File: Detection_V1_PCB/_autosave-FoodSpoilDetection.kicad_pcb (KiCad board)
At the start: 2 copper layers, 60 x 55 mm, 29 parts, among them J3 Conn_01x03_Socket, J4 Conn_01x03_Socket, J5 Conn_01x04_Socket, J6 Conn_01x03_Socket, J7 Conn_01x06_Socket, J9 Conn_01x10_Socket, Q1 AO3400A, Q2 AO3401A, Q3 AO3401A, U1 XIAO-ESP32-S3-DIP

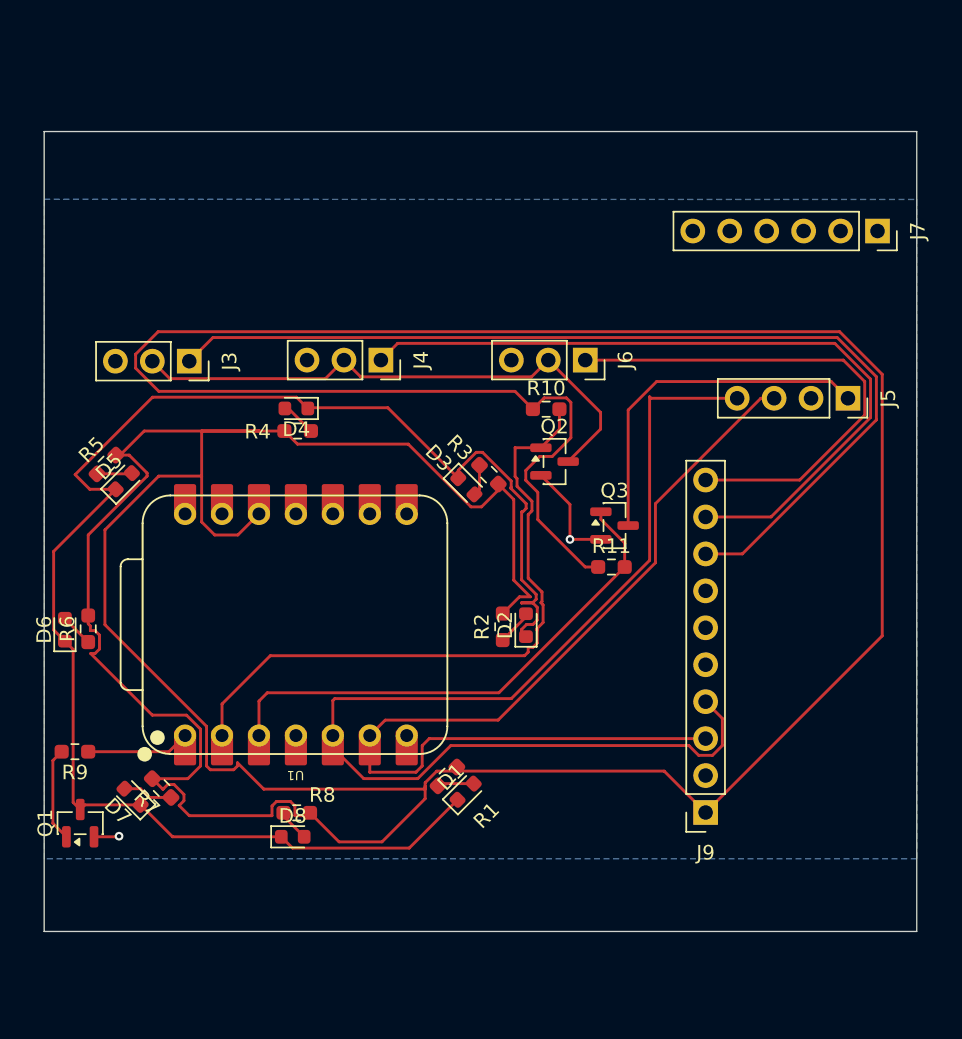
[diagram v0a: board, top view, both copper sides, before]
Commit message: added mounting holes
Need to align mounting holes and fiduciaries
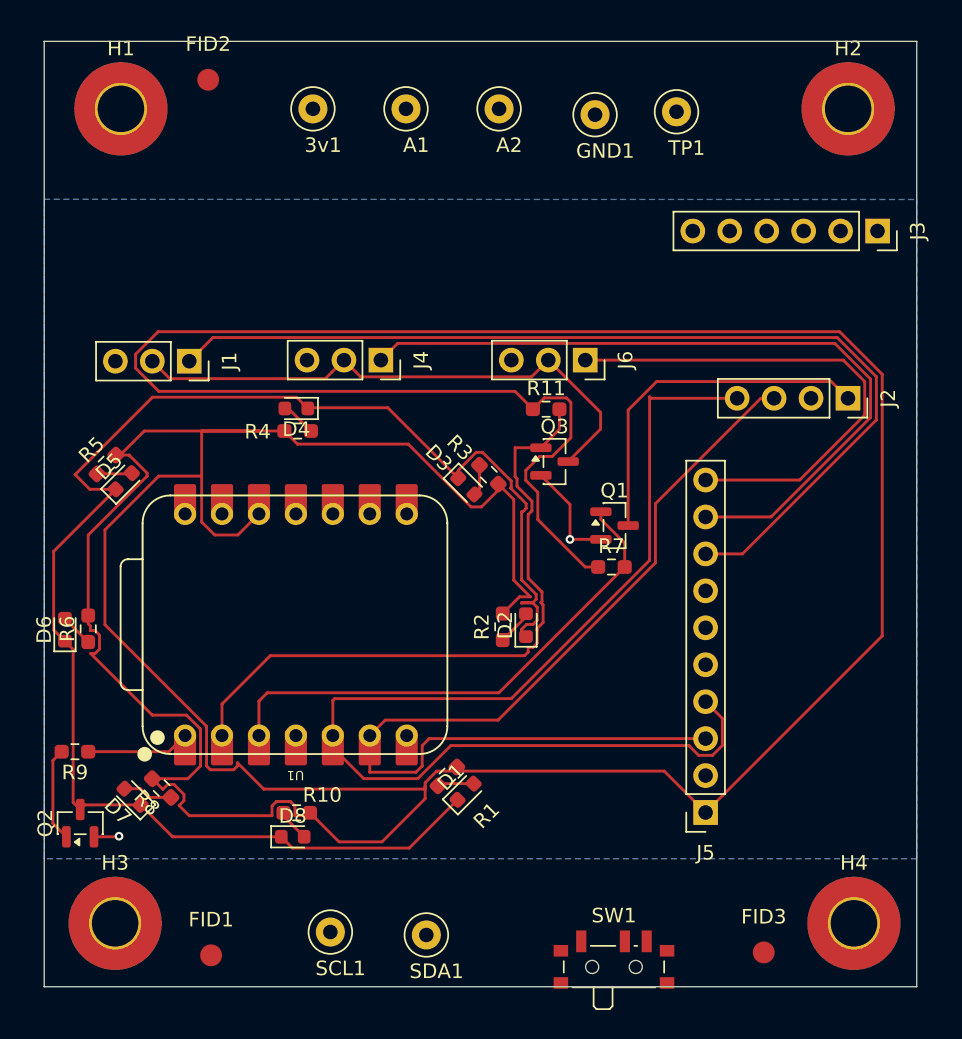
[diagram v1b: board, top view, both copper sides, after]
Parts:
- added 3v1: TestPoint, TestPoint:TestPoint_Loop_D1.80mm_Drill1.0mm_Beaded, F.Cu at (142.4, 73.6)
- added A1: TestPoint, TestPoint:TestPoint_Loop_D1.80mm_Drill1.0mm_Beaded, F.Cu at (148.8, 73.6)
- added A2: TestPoint, TestPoint:TestPoint_Loop_D1.80mm_Drill1.0mm_Beaded, F.Cu at (155.2, 73.6)
- added FID1: Fiducial, Fiducial:Fiducial_1.5mm_Mask3mm, F.Cu at (135.4, 131.8)
- added FID2: Fiducial, Fiducial:Fiducial_1.5mm_Mask3mm, F.Cu at (135.2, 71.6)
- added FID3: Fiducial, Fiducial:Fiducial_1.5mm_Mask3mm, F.Cu at (173.4, 131.6)
- added GND1: TestPoint, TestPoint:TestPoint_Loop_D1.80mm_Drill1.0mm_Beaded, F.Cu at (161.8, 74.0)
- added H1: MountingHole_Pad, MountingHole:MountingHole_3.2mm_M3_Pad_TopBottom, F.Cu at (129.2, 73.6)
- added H2: MountingHole_Pad, MountingHole:MountingHole_3.2mm_M3_Pad_TopBottom, F.Cu at (179.2, 73.6)
- added H3: MountingHole_Pad, MountingHole:MountingHole_3.2mm_M3_Pad_TopBottom, F.Cu at (128.8, 129.6)
- added H4: MountingHole_Pad, MountingHole:MountingHole_3.2mm_M3_Pad_TopBottom, F.Cu at (179.6, 129.6)
- added SCL1: TestPoint, TestPoint:TestPoint_Loop_D1.80mm_Drill1.0mm_Beaded, F.Cu at (143.6, 130.2)
- added SDA1: TestPoint, TestPoint:TestPoint_Loop_D1.80mm_Drill1.0mm_Beaded, F.Cu at (150.2, 130.4)
- added SW1: SW_DIP_x01, Button_Switch_SMD:SW_SPDT_PCM12, F.Cu at (163.1, 132.3)
- added TP1: A3, TestPoint:TestPoint_Loop_D1.80mm_Drill1.0mm_Beaded, F.Cu at (167.4, 73.8)
- renumbered J3 to J1, J5 to J2, J7 to J3, J9 to J5, Q3 to Q1, Q1 to Q2, Q2 to Q3, R8 to R10, R10 to R11, R11 to R7, R7 to R8
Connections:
- J5 pad 7: unconnected-(J9-Pin_7-Pad7) -> /A0
- Q1 pad 1: D2 -> D0
- R7 pad 2: D2 -> D0
- R9 pad 1: D0 -> D2
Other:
- board size 60 x 55 mm -> 60 x 65 mm
